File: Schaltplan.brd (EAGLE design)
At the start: 40.6 x 70.8 mm, 56 parts, among them Q1 TN0602N3, Q10 TN0602N3, Q11 TN0602N3, Q12 TN0602N3, Q13 TN0602N3, Q14 TN0602N3, Q15 TN0602N3, Q16 TN0602N3, Q17 TN0602N3, Q18 TN0602N3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

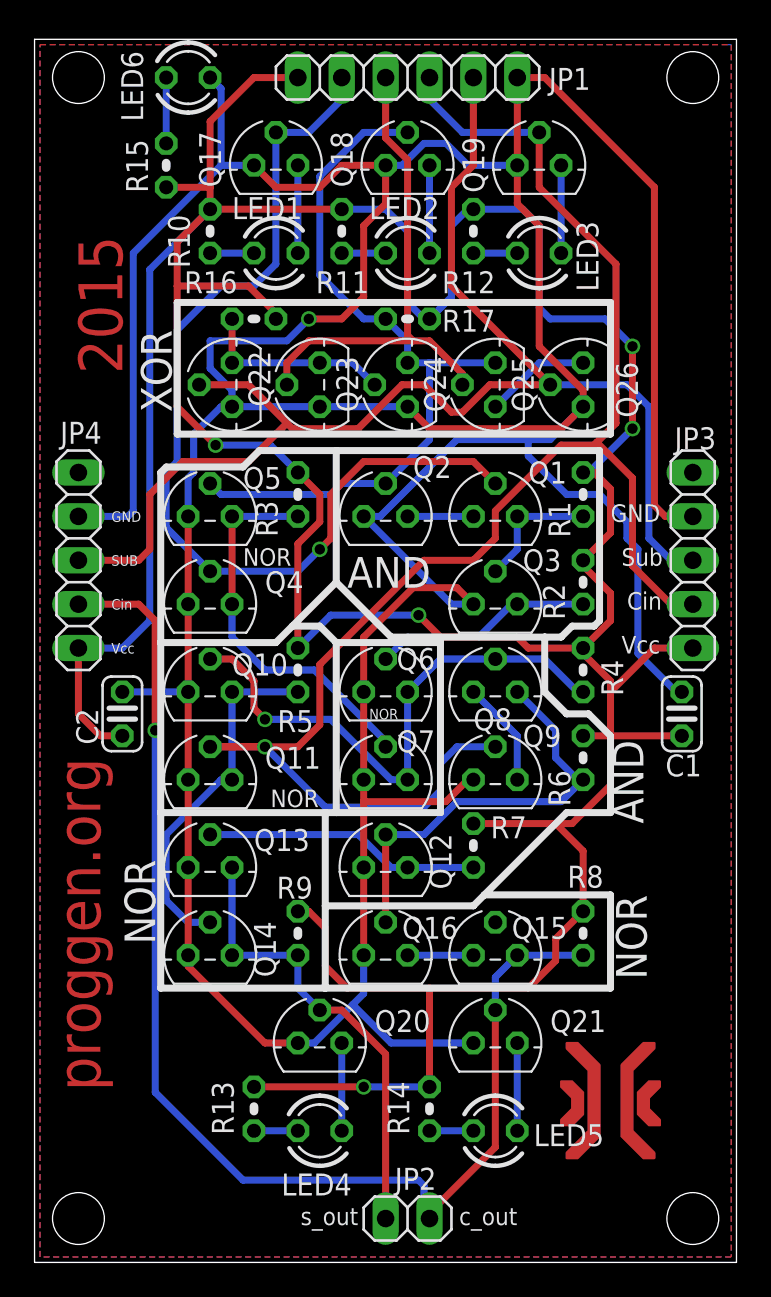
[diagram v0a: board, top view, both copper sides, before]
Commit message: Added Pull-Up Resistors
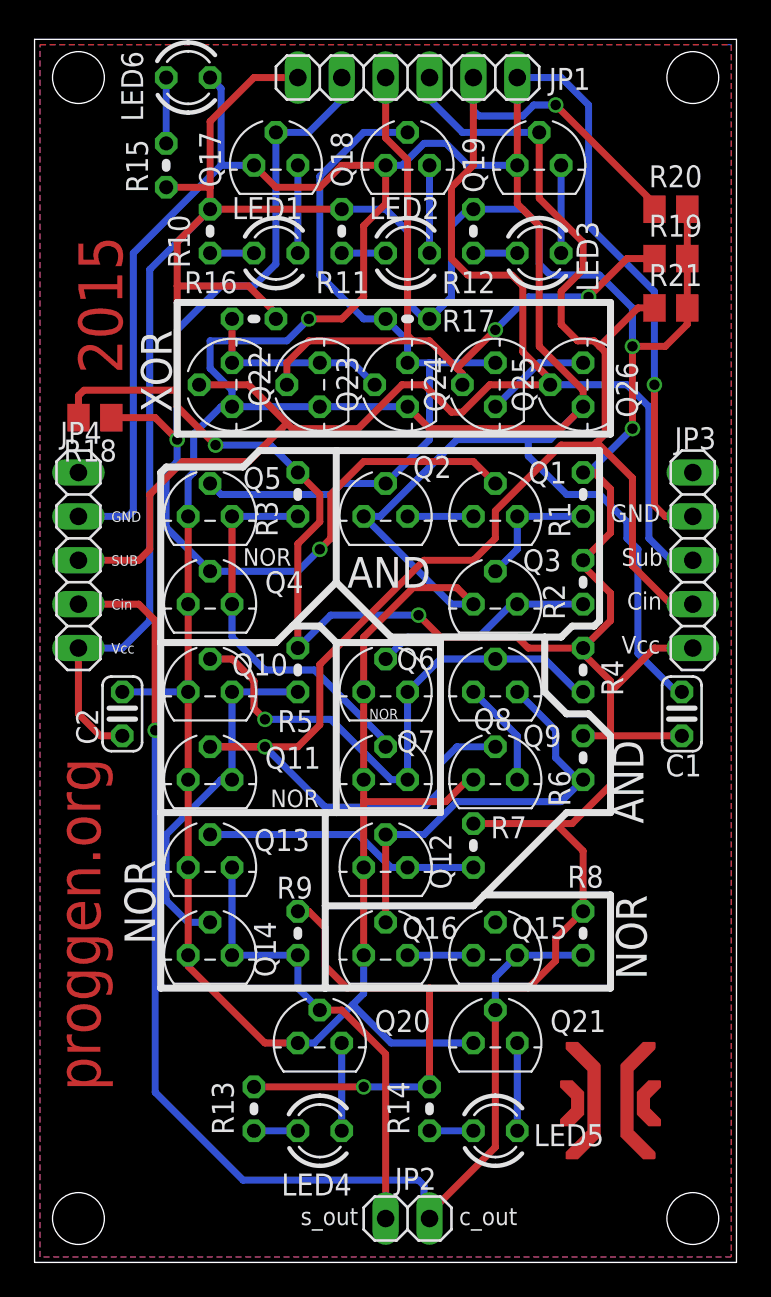
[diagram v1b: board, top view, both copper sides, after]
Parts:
- added R18, R19, R20, R21: 10k, resistor:M0805
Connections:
- net A: now also R18.1
- net B_IN: now also R19.1
- net C_IN: now also R21.1
- net SUB: now also R20.1
- net VCC: now also R18.2, R19.2, R20.2, R21.2
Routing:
- net VCC: track 242.7 -> 260.0 mm
- net SUB: track 78.6 -> 95.5 mm, vias 0 -> 1
- net B_IN: track 29.3 -> 43.3 mm, vias 0 -> 2
- net C_IN: track 94.1 -> 99.2 mm
- net A: track 57.2 -> 61.6 mm, vias 1 -> 2
- net GND: track 283.9 -> 284.4 mm, vias 1 -> 2
